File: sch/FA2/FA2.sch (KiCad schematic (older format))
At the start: 5 parts

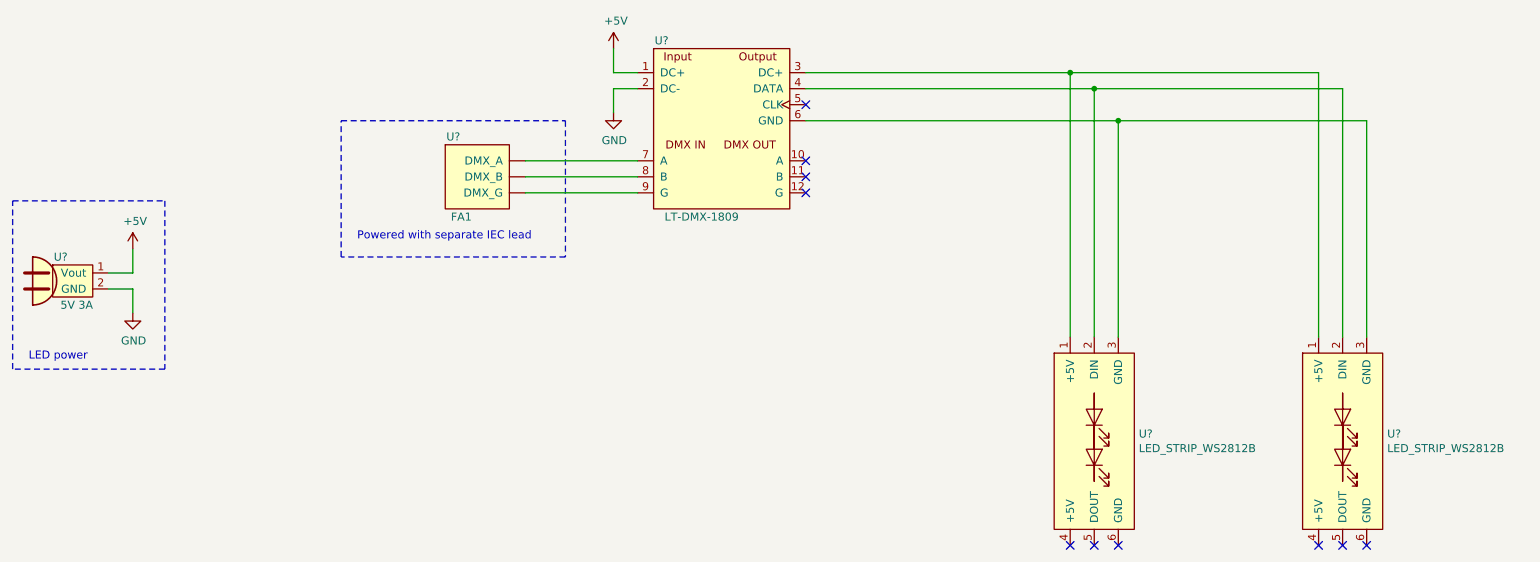
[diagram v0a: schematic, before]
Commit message: Completed BOMs and changed module connector name to 'Faraday_module'
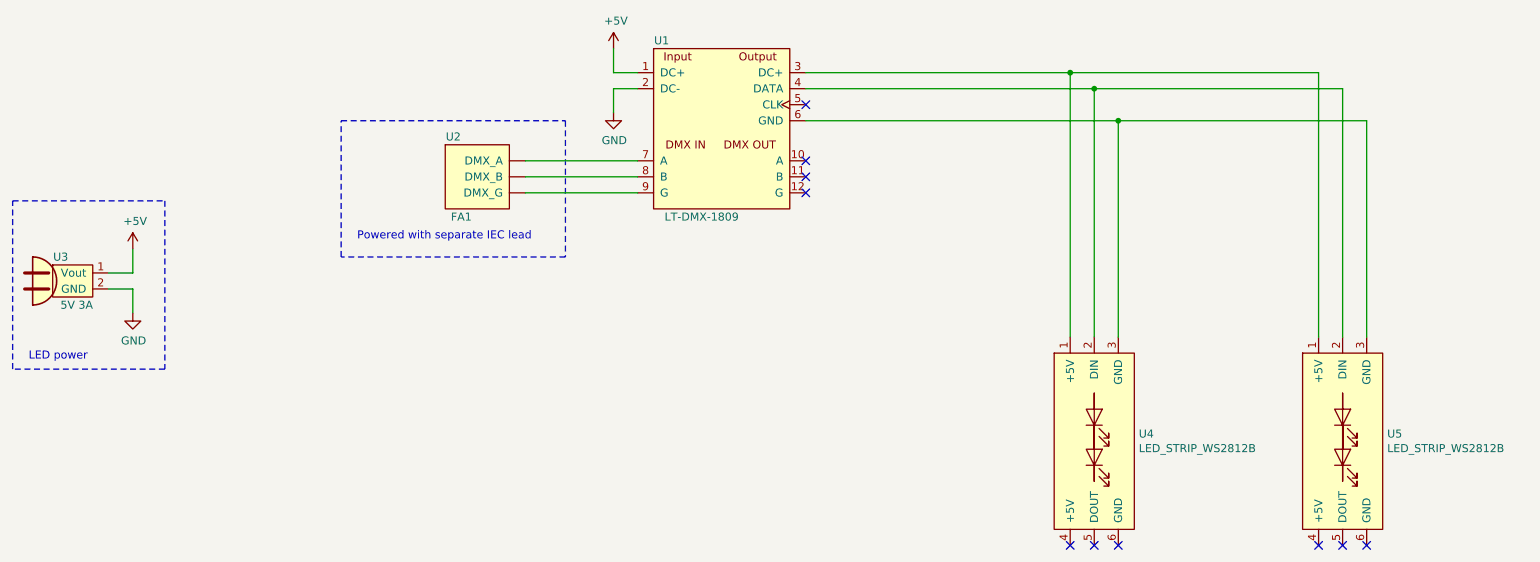
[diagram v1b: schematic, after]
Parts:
- removed U?: LED_STRIP_WS2812B, symbol faraday:LED_STRIP_WS2812B
- added U5: LED_STRIP_WS2812B, symbol faraday:LED_STRIP_WS2812B
- U1: renamed from U?; Description (none) -> DMX-512 Decoder SPI output 5-24VDC; Manufacturer (none) -> LTECH; Part Number (none) -> LT-DMX-1809; Supplier (none) -> Agoeu LED Express Store
- U2: renamed from U?; Description (none) -> FA1; Manufacturer (none) -> Newie Ventures
- U3: renamed from U?; Manufacturer (none) -> ?; Part Number (none) -> ?
- U4: renamed from U?; Description (none) -> 5M RGB LED Strip - WS2812 60 Per Meter - White Strip - Weat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; Order Number (none) -> CE04854; Supplier (none) -> Core Electronics
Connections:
- net at U1.3 (DC+), U4.1 (+5V): now also U5.1 (+5V)
- net at U1.4 (DATA), U4.2 (DIN): now also U5.2 (DIN)
- net at U1.6 (GND), U4.3 (GND): now also U5.3 (GND)
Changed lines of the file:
@@
 $EndBitmap
 $Comp
-L faraday:plugpack U?
+L faraday:plugpack U3
 U 1 1 5BBC3F5B
 P 1200 3850
-F 0 "U?" H 1150 4000 50  0000 C CNN
+F 0 "U3" H 1150 4000 50  0000 C CNN
 F 1 "5V 3A" H 1250 3700 50  0000 C CNN
 F 2 "" H 1100 3600 50  0001 C CNN
@@
 F 5 "MP-3480" H 1200 3850 50  0001 C CNN "Order Number"
 F 6 "AC adapter 110-240VAC to 5V 3A DC" H 1200 3850 50  0001 C CNN "Description"
+F 7 "?" H 1200 3850 50  0001 C CNN "Part Number"
+F 8 "?" H 1200 3850 50  0001 C CNN "Manufacturer"
 	1    1200 3850
 	1    0    0    -1
 $EndComp
 $Comp
-L faraday:FA1 U?
+L faraday:FA1 U2
 U 1 1 5BBC43B2
 P 3750 3200
-F 0 "U?" H 3600 3450 50  0000 C CNN
+F 0 "U2" H 3600 3450 50  0000 C CNN
 F 1 "FA1" H 3650 2950 50  0000 C CNN
 F 2 "" H 4350 3700 50  0001 C CNN
 F 3 "" H 4350 3700 50  0001 C CNN
+F 4 "FA1" H 3750 3200 50  0001 C CNN "Description"
+F 5 "Newie Ventures" H 3750 3200 50  0001 C CNN "Manufacturer"
 	1    3750 3200
 	1    0    0    -1
@@
 Powered with separate IEC lead
 $Comp
-L faraday:LED_STRIP_WS2812B U?
+L faraday:LED_STRIP_WS2812B U4
 U 1 1 5BC830D0
 P 7600 4850
-F 0 "U?" H 7878 4896 50  0000 L CNN
+F 0 "U4" H 7878 4896 50  0000 L CNN
 F 1 "LED_STRIP_WS2812B" H 7878 4805 50  0000 L CNN
 F 2 "" V 7800 4950 50  0001 C CNN
 F 3 "" V 7800 4950 50  0001 C CNN
+F 4 "CE04854" H 7600 4850 50  0001 C CNN "Order Number"
+F 5 "Core Electronics" H 7600 4850 50  0001 C CNN "Supplier"
+F 6 "5M RGB LED Strip - WS2812 60 Per Meter - White Strip - Weatherproof" H 7600 4850 50  0001 C CNN "Description"
 	1    7600 4850
-	1    0    0    -1
-$EndComp
-$Comp
-L faraday:LED_STRIP_WS2812B U?
-U 1 1 5BC831F6
-P 9150 4850
-F 0 "U?" H 9428 4896 50  0000 L CNN
-F 1 "LED_STRIP_WS2812B" H 9428 4805 50  0000 L CNN
-F 2 "" V 9350 4950 50  0001 C CNN
-F 3 "" V 9350 4950 50  0001 C CNN
-	1    9150 4850
 	1    0    0    -1
 $EndComp
@@
 	1600 3900 1600 4050
 $Comp
-L power:GND #PWR?
+L power:GND #PWR04
 U 1 1 5BC83548
 P 1600 4050
-F 0 "#PWR?" H 1600 3800 50  0001 C CNN
+F 0 "#PWR04" H 1600 3800 50  0001 C CNN
 F 1 "GND" H 1605 3877 50  0000 C CNN
 F 2 "" H 1600 4050 50  0001 C CNN
@@
 $EndComp
 $Comp
-L power:+5V #PWR?
+L power:+5V #PWR03
 U 1 1 5BC835A0
 P 1600 3650
-F 0 "#PWR?" H 1600 3500 50  0001 C CNN
+F 0 "#PWR03" H 1600 3500 50  0001 C CNN
 F 1 "+5V" H 1615 3823 50  0000 C CNN
 F 2 "" H 1600 3650 50  0001 C CNN
@@
 NoConn ~ 9300 5500
 $Comp
-L faraday:LT-DMX-1809 U?
+L faraday:LT-DMX-1809 U1
 U 1 1 5BC843BC
 P 5250 2750
-F 0 "U?" H 4900 3150 50  0000 C CNN
+F 0 "U1" H 4900 3150 50  0000 C CNN
 F 1 "LT-DMX-1809" H 5150 2050 50  0000 C CNN
 F 2 "" H 6100 3500 50  0001 C CNN
 F 3 "" H 6100 3500 50  0001 C CNN
+F 4 "LT-DMX-1809" H 5250 2750 50  0001 C CNN "Part Number"
+F 5 "LTECH" H 5250 2750 50  0001 C CNN "Manufacturer"
+F 6 "DMX-512 Decoder SPI output 5-24VDC" H 5250 2750 50  0001 C CNN "Description"
+F 7 "Agoeu LED Express Store" H 5250 2750 50  0001 C CNN "Supplier"
 	1    5250 2750
 	1    0    0    -1
@@
 	4600 2550 4600 2400
 $Comp
-L power:+5V #PWR?
+L power:+5V #PWR01
 U 1 1 5BC84768
 P 4600 2400
-F 0 "#PWR?" H 4600 2250 50  0001 C CNN
+F 0 "#PWR01" H 4600 2250 50  0001 C CNN
 F 1 "+5V" H 4615 2573 50  0000 C CNN
 F 2 "" H 4600 2400 50  0001 C CNN
@@
 	4600 2650 4600 2800
 $Comp
-L power:GND #PWR?
+L power:GND #PWR02
 U 1 1 5BC848A6
 P 4600 2800
-F 0 "#PWR?" H 4600 2550 50  0001 C CNN
+F 0 "#PWR02" H 4600 2550 50  0001 C CNN
 F 1 "GND" H 4605 2627 50  0000 C CNN
 F 2 "" H 4600 2800 50  0001 C CNN
@@
 NoConn ~ 5800 3200
 NoConn ~ 5800 3300
+$Comp
+L faraday:LED_STRIP_WS2812B U5
+U 1 1 5BC9372E
+P 9150 4850
+F 0 "U5" H 9428 4896 50  0000 L CNN
+F 1 "LED_STRIP_WS2812B" H 9428 4805 50  0000 L CNN
+F 2 "" V 9350 4950 50  0001 C CNN
+F 3 "" V 9350 4950 50  0001 C CNN
+F 4 "CE04854" H 9150 4850 50  0001 C CNN "Order Number"
+F 5 "Core Electronics" H 9150 4850 50  0001 C CNN "Supplier"
+F 6 "5M RGB LED Strip - WS2812 60 Per Meter - White Strip - Weatherproof" H 9150 4850 50  0001 C CNN "Description"
+	1    9150 4850
+	1    0    0    -1
+$EndComp
 $EndSCHEMATC
